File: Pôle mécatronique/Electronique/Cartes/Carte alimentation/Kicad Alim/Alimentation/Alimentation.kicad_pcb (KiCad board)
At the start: 2 copper layers, 65 x 90 mm, 27 parts, among them J1 Conn_01x04, J2 Conn_01x04, J3 Conn_01x04, J4 Conn_01x05, J5 Conn_01x05, J6 Conn_02x03_Odd_Even, J7 Conn_02x10_Odd_Even, J8 24V in, J9 24V out, K1 G5LE-1, Q1 BD135, SW1 SW_DPDT_x2, U1 TSR_2-2450, U2 TSR_2-2450, U3 TSR_2-24120

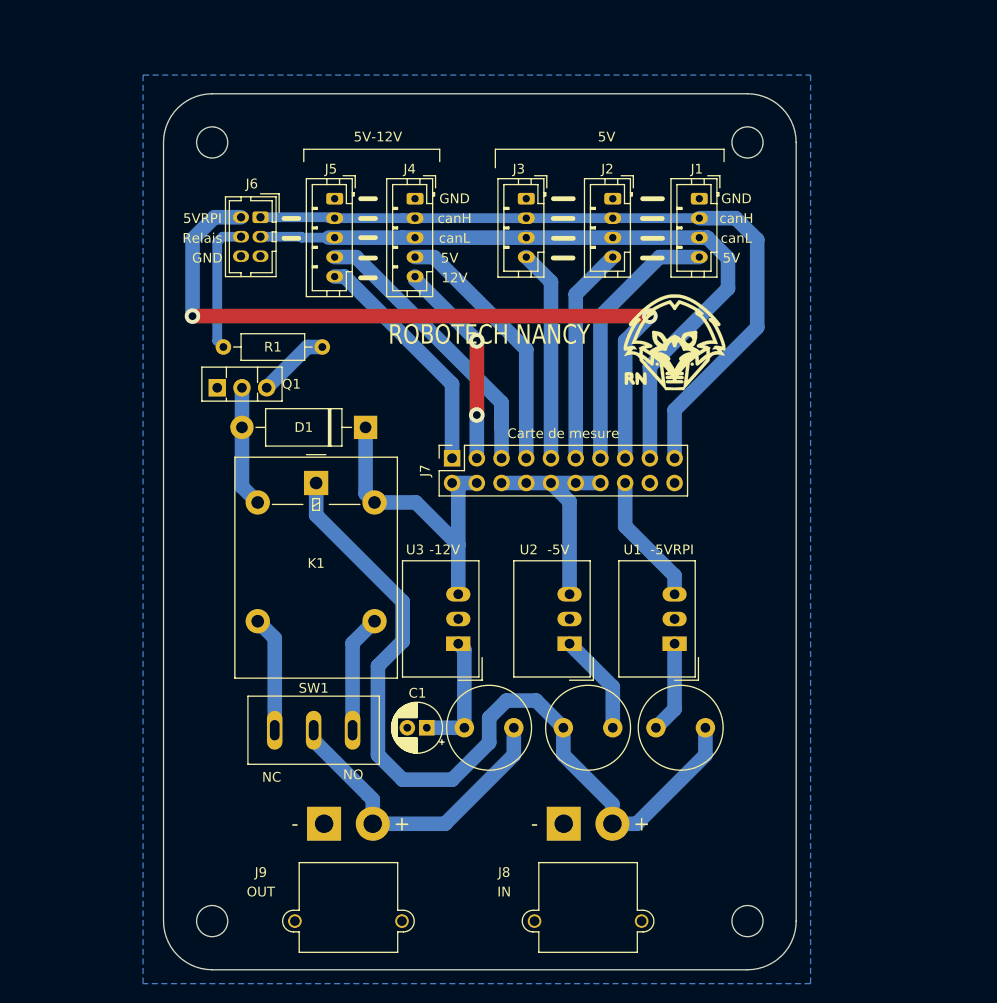
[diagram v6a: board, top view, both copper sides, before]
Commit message: Update alim
- Ajout de la connexion du bus can à la BR
- Normalisation des perçages
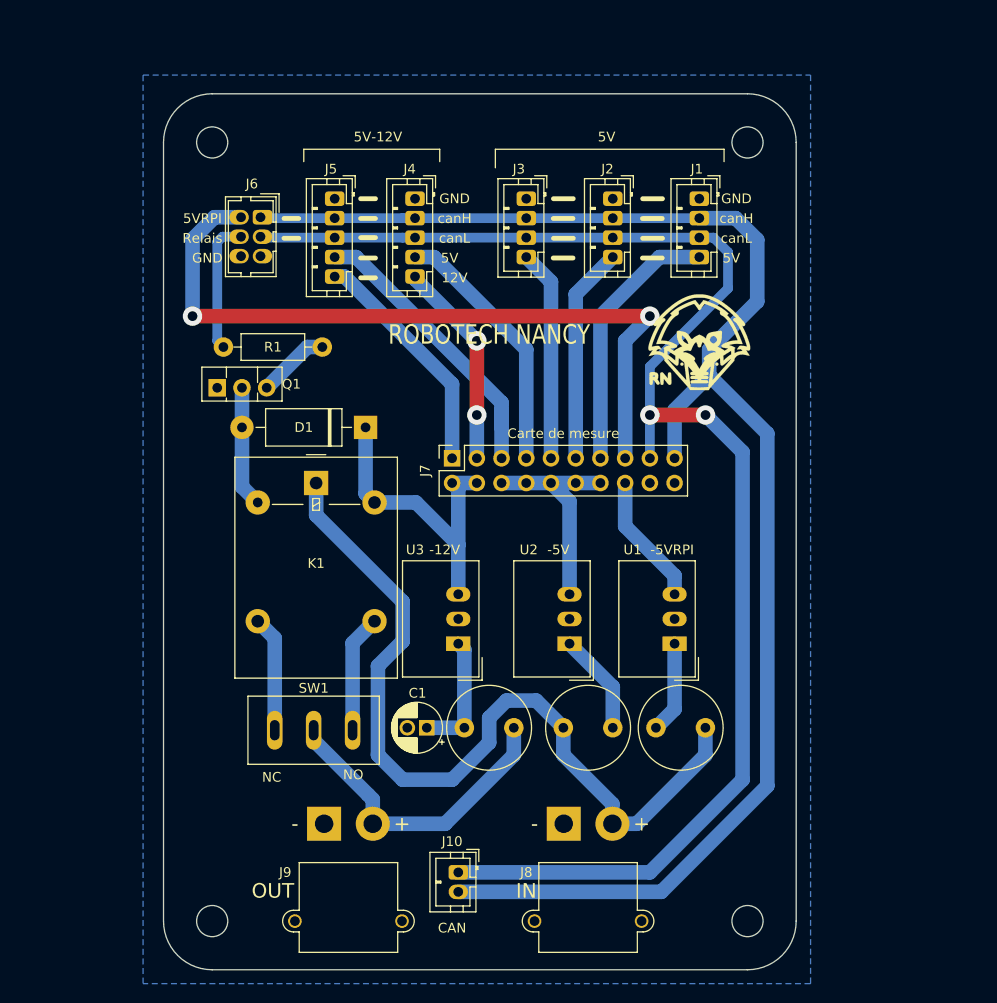
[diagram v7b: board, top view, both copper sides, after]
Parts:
- added J10: 24V in, Connector_JST:JST_PH_B2B-PH-K_1x02_P2.00mm_Vertical, F.Cu at (118.2, 115.4)
- moved G*** 2.54 mm to (143.0, 60.8) (x2)
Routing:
- net can_H: track 78.6 -> 158.7 mm
- net can_L: track 73.5 -> 151.6 mm, vias 0 -> 2
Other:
- board text added: "CAN"

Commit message: Correction pcb BR
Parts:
- added R2: 120, Resistor_THT:R_Axial_DIN0207_L6.3mm_D2.5mm_P10.16mm_Horizontal, F.Cu at (123.7, 122.7)
- added R3: 120, Resistor_THT:R_Axial_DIN0207_L6.3mm_D2.5mm_P10.16mm_Horizontal, F.Cu at (100.8, 44.2)
- added TP1: TestPoint, TestPoint:TestPoint_Pad_D2.0mm, B.Cu at (146.8, 81.8)
- added TP2: TestPoint, TestPoint:TestPoint_Pad_D2.0mm, B.Cu at (149.9, 81.8)
- added TP3: TestPoint, TestPoint:TestPoint_Pad_D2.0mm, B.Cu at (96.0, 74.2)
- added TP4: TestPoint, TestPoint:TestPoint_Pad_D2.0mm, B.Cu at (108.7, 74.2)
- added TP5: TestPoint, TestPoint:TestPoint_Pad_D2.0mm, B.Cu at (107.4, 94.0)
- added TP6: TestPoint, TestPoint:TestPoint_Pad_D2.0mm, B.Cu at (98.6, 82.0)
- added TP7: TestPoint, TestPoint:TestPoint_Pad_D2.0mm, B.Cu at (99.3, 94.0)
- added TP8: TestPoint, TestPoint:TestPoint_Pad_D2.0mm, B.Cu at (94.0, 58.7)
- added TP9: TestPoint, TestPoint:TestPoint_Pad_D2.0mm, B.Cu at (101.1, 63.2)
- moved J10 2.48 mm to (119.4, 117.6)
- moved J8 1.48 mm to (130.6, 110.4)
- moved J5 1.02 mm to (106.6, 46.2)
- moved J4 0.76 mm to (114.6, 46.2)
- moved J6 0.64 mm to (97.3, 48.1)
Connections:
- F2 pad 2: Vbatt -> VbattRelay
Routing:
- net Vbatt: track 86.0 -> 100.8 mm
- net can_L: track 151.6 -> 158.8 mm
- net VbattRelay: track 32.3 -> 37.4 mm
- net can_H: track 158.7 -> 163.1 mm
- net 5Vout5: track 30.9 -> 29.9 mm
- net 12Vout2: track 24.3 -> 23.2 mm
- net 5Vout4: track 26.5 -> 25.8 mm
- net 5VRPI: track 76.5 -> 75.8 mm
- net GND: vias 0 -> 20
- added copper zone on F.Cu, net GND
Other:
- board text added: "+Bobine relais"
- board text added: "Base Transistor"
- board text added: "CanH"
- board text added: "CanL"
- board text added: "Cmd Relais"
- board text added: "Vbatt"
